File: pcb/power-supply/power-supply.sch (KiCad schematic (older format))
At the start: 25 parts, among them J1 Conn_01x20_Female, J2 Conn_01x20_Female, J3 Conn_02x03, J4 Conn_01x03, J5 Conn_01x02, J6 Conn_01x02, J7 Conn_01x02, J8 Conn_01x02

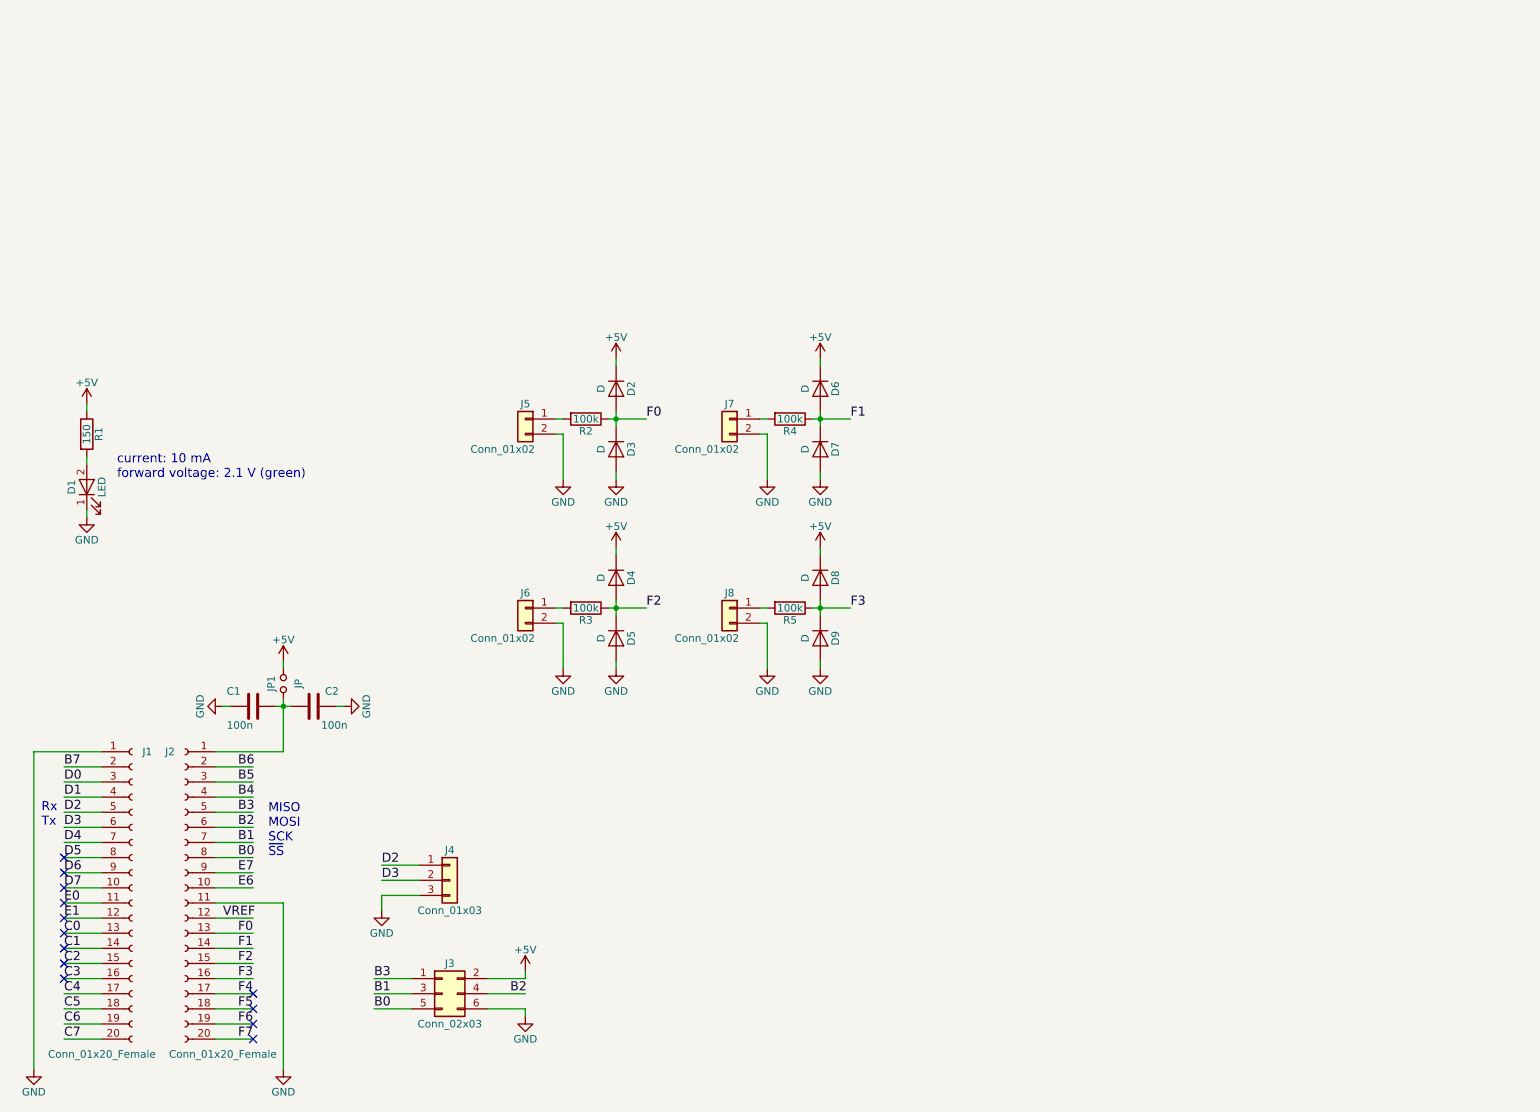
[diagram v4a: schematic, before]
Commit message: added the teensy schematic and footprint lib to the project, added the project from mr veigl to git, added teensy++2.0 to the schematic, added molex connectors, 02x05 pinheaders for motor control signals
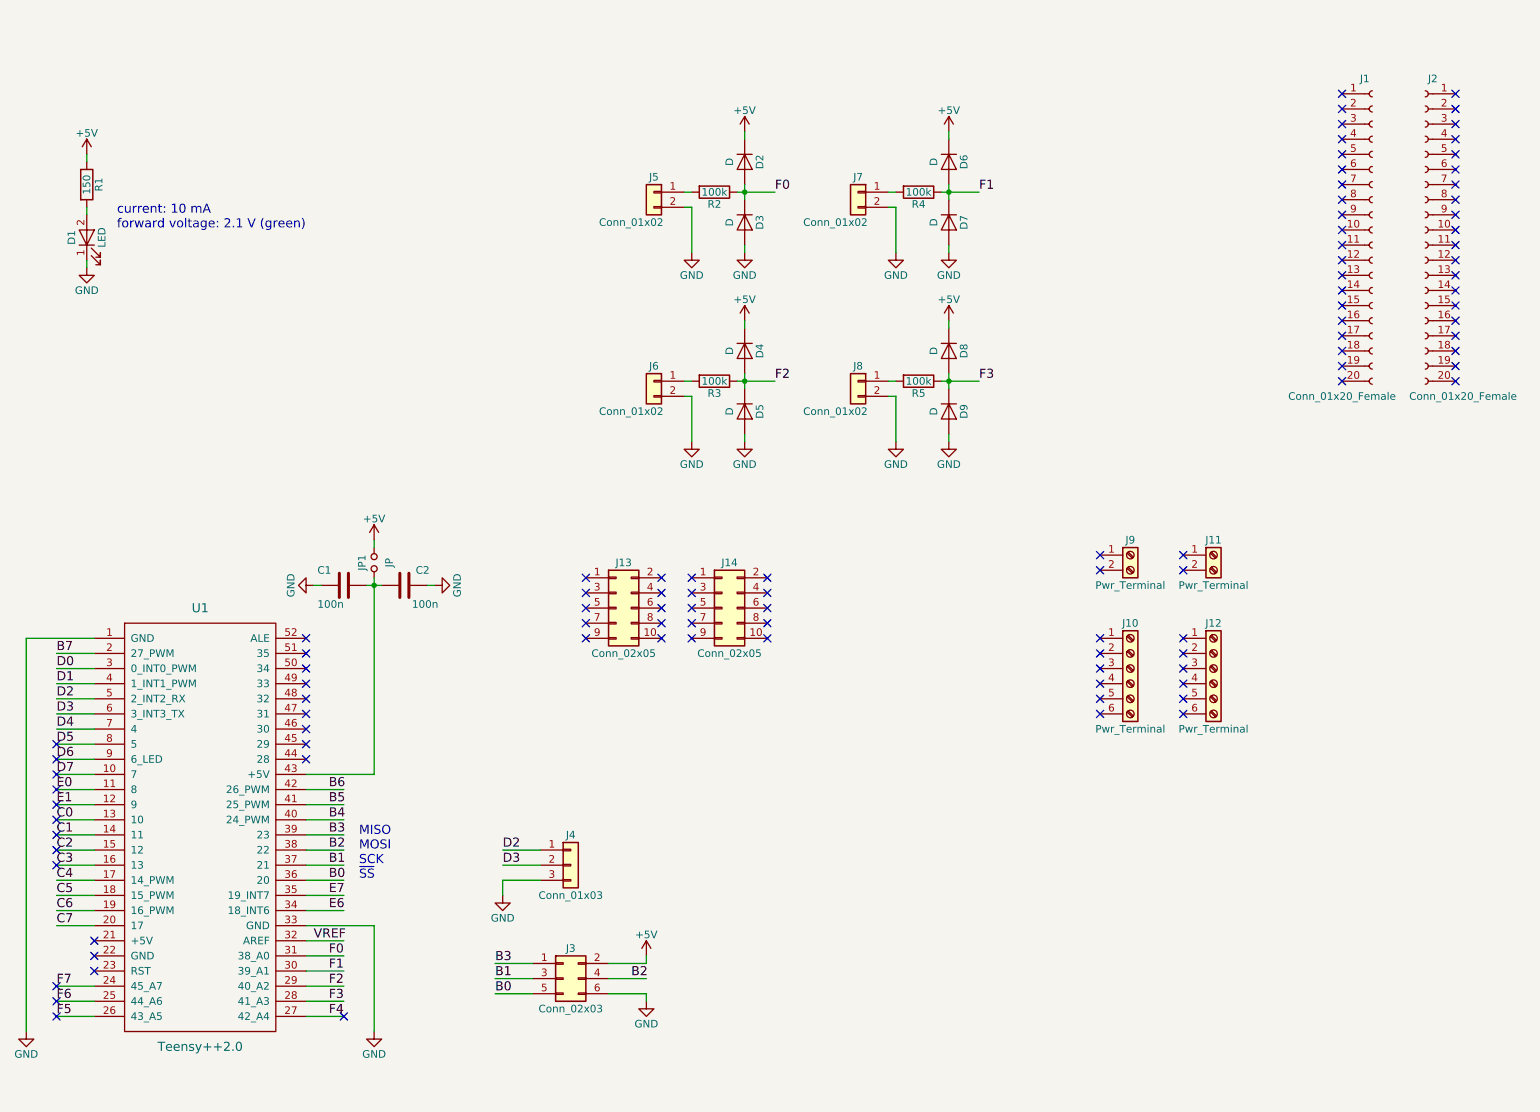
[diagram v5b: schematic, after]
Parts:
- added J10, J12: Pwr_Terminal, Connectors_Molex:Molex_MiniFit-JR-5556-06A_2x03x4.20mm_Straight, symbol Screw_Terminal_01x06
- added J11, J9: Pwr_Terminal, Connectors_Molex:Molex_MiniFit-JR-5556-02B_2x01x4.20mm_Straight, symbol Screw_Terminal_01x02
- added J13, J14: Conn_02x05, Pin_Headers:Pin_Header_Straight_2x05_Pitch2.54mm, symbol Conn_02x05_Odd_Even
- added U1: Teensy++2.0, Teensy:Teensy2.0++, symbol Teensy++2.0
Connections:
- no-connect marks 13 -> 101
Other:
- note removed: "Rx\nTx"
- moved on the sheet: C1, C2, D1, D2, D3, D4, D5, D6, D7, D8, D9, J1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

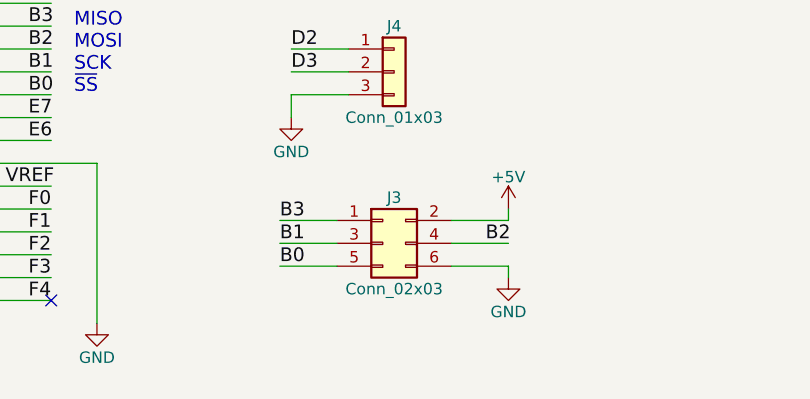
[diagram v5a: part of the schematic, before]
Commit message: changed the 02x03 spi connector to a 02x05 connector with \CS
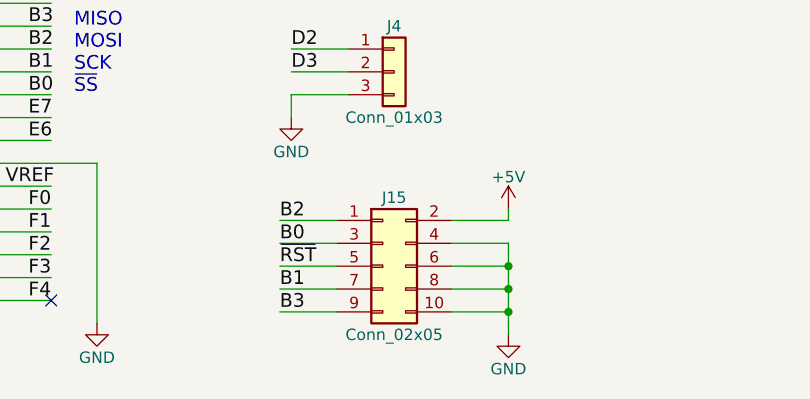
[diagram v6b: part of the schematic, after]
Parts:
- removed J3: Conn_02x03, Pin_Headers:Pin_Header_Straight_2x03_Pitch2.54mm, symbol Conn_02x03_Odd_Even
- added J15: Conn_02x05, Pin_Headers:Pin_Header_Straight_2x05_Pitch2.54mm, symbol Conn_02x05_Odd_Even
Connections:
- net labels added: ~RST
- wire segments 94 -> 98
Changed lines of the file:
@@
 	1    0    0    -1
 $EndComp
-$Comp
-L Conn_02x03_Odd_Even J3
-U 1 1 5B076301
-P 4500 6950
-F 0 "J3" H 4550 7150 50  0000 C CNN
-F 1 "Conn_02x03" H 4550 6750 50  0000 C CNN
-F 2 "Pin_Headers:Pin_Header_Straight_2x03_Pitch2.54mm" H 4500 6950 50  0001 C CNN
-F 3 "" H 4500 6950 50  0001 C CNN
-	1    4500 6950
-	1    0    0    -1
-$EndComp
-Wire Wire Line
-	4300 6850 4050 6850
 Wire Wire Line
 	4300 6950 4050 6950
-Wire Wire Line
-	4300 7050 4050 7050
-Wire Wire Line
-	4800 6850 5050 6850
-Wire Wire Line
-	4800 6950 5050 6950
-Wire Wire Line
-	4800 7050 5050 7050
 Text Notes 3150 6300 0    60   ~ 0
 MISO\nMOSI\nSCK\n~SS
+Text Label 4050 7250 0    60   ~ 0
+B3
+Text Label 4050 7150 0    60   ~ 0
+B1
+Text Label 4050 6950 0    60   ~ 0
+B0
 Text Label 4050 6850 0    60   ~ 0
-B3
-Text Label 4050 6950 0    60   ~ 0
-B1
-Text Label 4050 7050 0    60   ~ 0
-B0
-Text Label 4950 6950 0    60   ~ 0
 B2
 $Comp
 L GND #PWR021
 U 1 1 5B076D3D
-P 5050 7100
-F 0 "#PWR021" H 5050 6850 50  0001 C CNN
-F 1 "GND" H 5050 6950 50  0000 C CNN
-F 2 "" H 5050 7100 50  0001 C CNN
-F 3 "" H 5050 7100 50  0001 C CNN
-	1    5050 7100
+P 5050 7350
+F 0 "#PWR021" H 5050 7100 50  0001 C CNN
+F 1 "GND" H 5050 7200 50  0000 C CNN
+F 2 "" H 5050 7350 50  0001 C CNN
+F 3 "" H 5050 7350 50  0001 C CNN
+	1    5050 7350
 	1    0    0    -1
 $EndComp
@@
 Wire Wire Line
 	5050 6850 5050 6800
-Wire Wire Line
-	5050 7050 5050 7100
 $Comp
 L Conn_01x03 J4
@@
 NoConn ~ 5850 4600
 NoConn ~ 5850 4700
+Wire Wire Line
+	4300 6850 4050 6850
+Wire Wire Line
+	4050 7050 4300 7050
+Wire Wire Line
+	4300 7150 4050 7150
+Wire Wire Line
+	4800 6850 5050 6850
+Wire Wire Line
+	4800 6950 5050 6950
+Wire Wire Line
+	4800 7050 5050 7050
+Wire Wire Line
+	5050 7150 4800 7150
+Wire Wire Line
+	5050 6950 5050 7350
+Connection ~ 5050 7050
+Connection ~ 5050 7150
+$Comp
+L Conn_02x05_Odd_Even J15
+U 1 1 5B07889D
+P 4500 7050
+F 0 "J15" H 4550 7350 50  0000 C CNN
+F 1 "Conn_02x05" H 4550 6750 50  0000 C CNN
+F 2 "Pin_Headers:Pin_Header_Straight_2x05_Pitch2.54mm" H 4500 7050 50  0001 C CNN
+F 3 "" H 4500 7050 50  0001 C CNN
+	1    4500 7050
+	1    0    0    -1
+$EndComp
+Text Label 4050 7050 0    60   ~ 0
+~RST
+Wire Wire Line
+	4300 7250 4050 7250
+Wire Wire Line
+	4800 7250 5050 7250
+Connection ~ 5050 7250
 $EndSCHEMATC
